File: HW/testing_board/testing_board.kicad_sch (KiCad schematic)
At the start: 66 parts, among them J1 GPIO, J4 Left_, J4 SWD, J5 OLED, J5 Right_, SW1 Start, U1 TPS22917DBV, U2 CD4051BM96, U3 CD4051BM96, U4 CD4051BM96

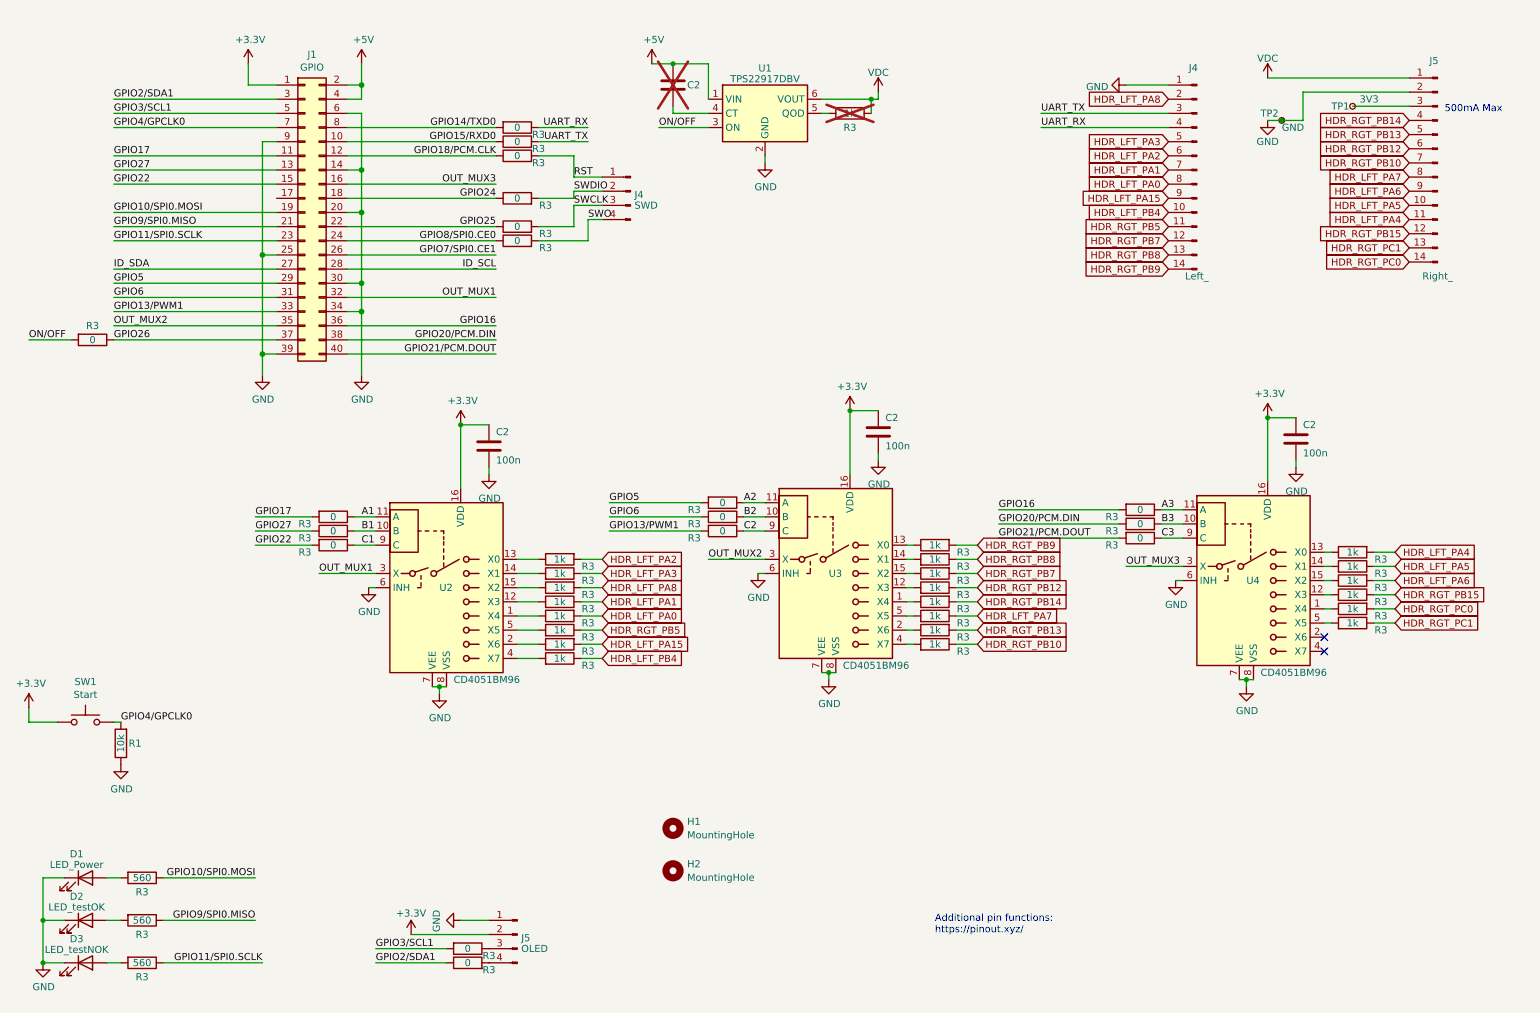
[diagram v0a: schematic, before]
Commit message: add sd card file library+ new HW version
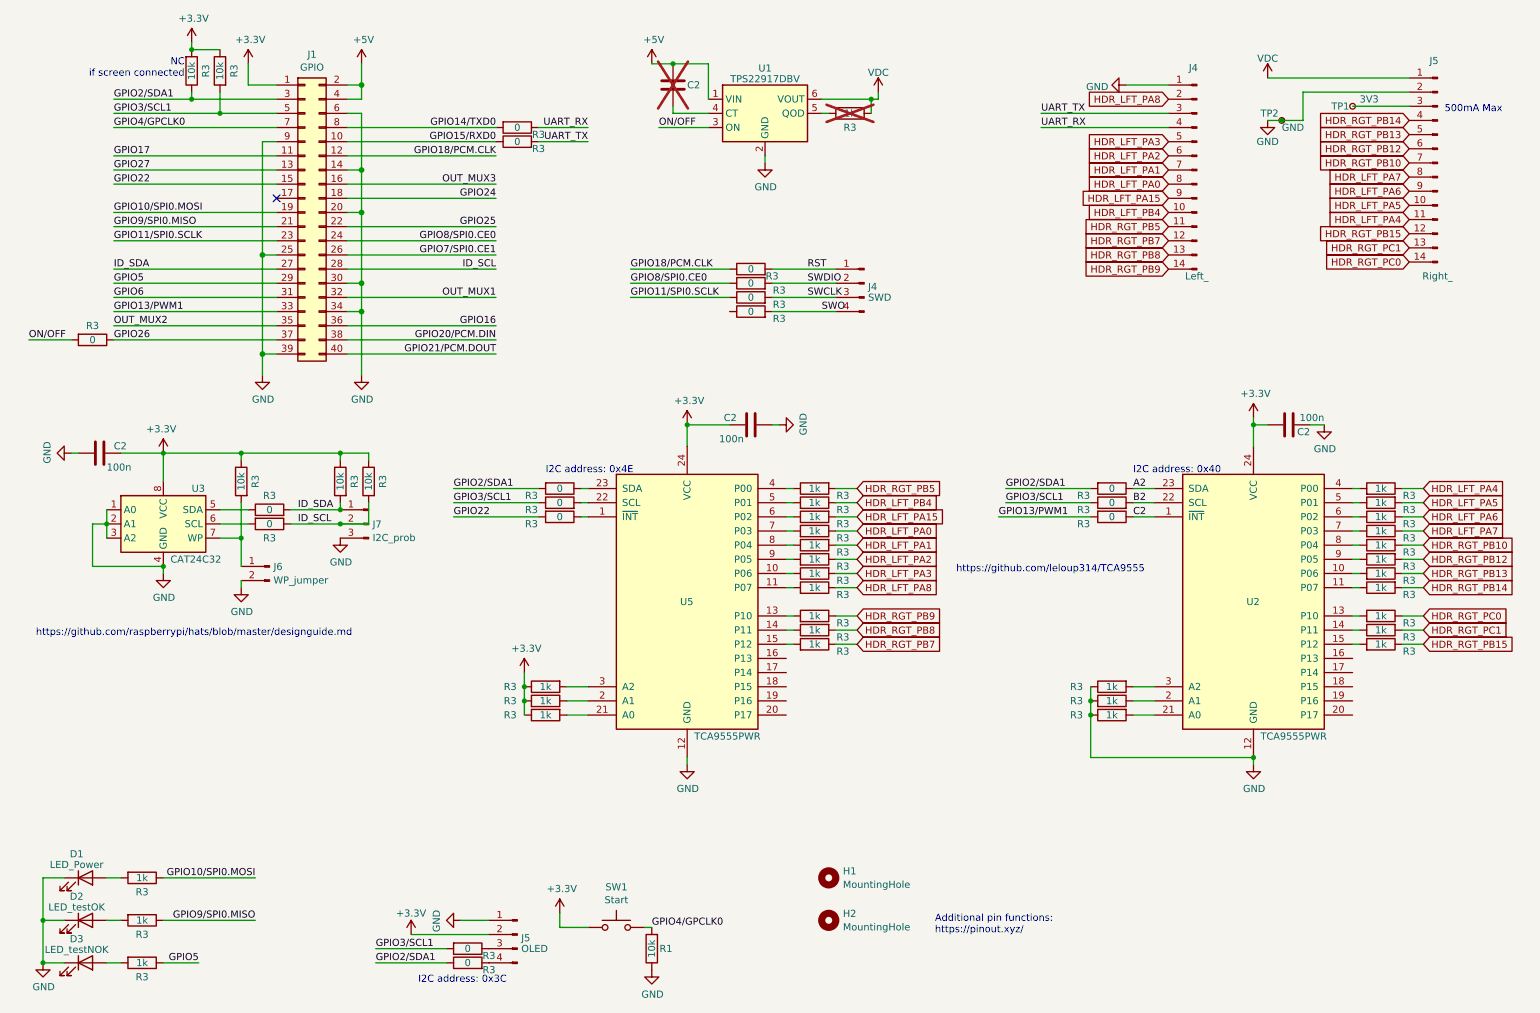
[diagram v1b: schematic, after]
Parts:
- removed R3 (x3): 0, Resistor_SMD:R_0603_1608Metric, symbol Device:R
- removed R3 (x2): 560, Resistor_SMD:R_0603_1608Metric, symbol Device:R
- removed U2, U3, U4: CD4051BM96, Package_SO:SOIC-16_3.9x9.9mm_P1.27mm, symbol Analog_Switch:CD4051B
- added J6: WP_jumper, Connector_PinHeader_2.54mm:PinHeader_1x02_P2.54mm_Vertical, symbol Connector:Conn_01x02_Pin
- added J7: I2C_prob, Connector_PinHeader_2.54mm:PinHeader_1x03_P2.54mm_Vertical, symbol Connector:Conn_01x03_Pin
- added R3 (x5): 10k, Resistor_SMD:R_0603_1608Metric, symbol Device:R
- added R3 (x8): 1k, Resistor_SMD:R_0603_1608Metric, symbol Device:R
- added R3 (x2): 0, Resistor_SMD:R_0603_1608Metric, symbol Device:R
- added U2, U5: TCA9555PWR, Package_SO:TSSOP-24_4.4x7.8mm_P0.65mm, symbol Interface_Expansion:TCA9555PWR
- added U3: CAT24C32, Package_SO:SOIC-8_3.9x4.9mm_P1.27mm, symbol Memory_EEPROM:CAT24C128
- R3: value 560 -> 1k
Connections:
- net +3V3: now also R3.1, R3.1, R3.1, R3.1, R3.1, R3.1, R3.2, R3.2, U2.24 (VCC), U3.8 (VCC), U5.24 (VCC)
- net A2: now also U2.23 (SDA)
- net B2: now also U2.22 (SCL)
- net C2: now also U2.1 (~{INT})
- net GND: now also J6.2 (Pin_2), J7.3 (Pin_3), R3.1, R3.1, R3.2, U2.12 (GND), U3.1 (A0), U3.2 (A1), U3.3 (A2), U3.4 (GND), U5.12 (GND)
- net GPIO11/SPI0.SCLK: now also R3.1
- net GPIO17: no longer R3.2
- net GPIO24: no longer R3.1
- net GPIO25: no longer R3.1
- net GPIO27: no longer R3.1
- net GPIO2/SDA1: now also R3.2, R3.2, R3.1
- net GPIO3/SCL1: now also R3.1, R3.1, R3.2
- net GPIO5: now also R3.1; no longer R3.2
- net GPIO6: no longer R3.1
- net GPIO8/SPI0.CE0: now also R3.1; no longer R3.1
- net GPIO9/SPI0.MISO: now also R3.1
- net HDR_LFT_PA0: now also R3.1; no longer R3.2
- net HDR_LFT_PA1: now also R3.2; no longer R3.1
- net HDR_LFT_PA15: now also R3.2; no longer R3.2
- net HDR_LFT_PA2: now also R3.1; no longer R3.2
- net HDR_LFT_PA3: now also R3.2; no longer R3.1
- net HDR_LFT_PA4: now also R3.1; no longer R3.2
- net HDR_LFT_PA5: now also R3.2; no longer R3.1
- net HDR_LFT_PA6: now also R3.2; no longer R3.2
- net HDR_LFT_PA7: now also R3.1; no longer R3.1
- net HDR_LFT_PA8: now also R3.1; no longer R3.2
- net HDR_LFT_PB4: now also R3.1; no longer R3.1
- net HDR_RGT_PB10: now also R3.2; no longer R3.1
- net HDR_RGT_PB12: now also R3.2; no longer R3.1
- net HDR_RGT_PB13: now also R3.1; no longer R3.2
- net HDR_RGT_PB14: now also R3.2; no longer R3.2
- net HDR_RGT_PB15: now also R3.1; no longer R3.1
- net HDR_RGT_PB5: now also R3.2; no longer R3.1
- net HDR_RGT_PB7: now also R3.1; no longer R3.2
- net HDR_RGT_PB8: now also R3.2; no longer R3.1
- net HDR_RGT_PB9: now also R3.1; no longer R3.2
- net HDR_RGT_PC0: now also R3.1; no longer R3.2
- net HDR_RGT_PC1: now also R3.2; no longer R3.1
- net ID_SCL: now also J7.2 (Pin_2), R3.1, R3.2
- net ID_SDA: now also J7.1 (Pin_1), R3.2, R3.2
- net at R3.1: now also U5.6 (P02)
- net at R3.2: now also U5.11 (P07)
- net at R3.2: now also U5.5 (P01)
- net at R3.1: now also U2.14 (P11)
- net at R3.1: now also U2.5 (P01)
- net at R3.2: now also U2.4 (P00)
- net at R3.1: now also U2.6 (P02)
- net at R3.2: now also U2.7 (P03)
- net at R3.1: now also U2.8 (P04)
- net at R3.1: now also U5.14 (P11)
- net at R3.2: now also U5.15 (P12)
- net at R3.2: now also U5.13 (P10)
- net at R3.2: now also U5.7 (P03)
- net at R3.1: now also U5.8 (P04)
- net at R3.2: now also U2.13 (P10)
- net at R3.2: now also U2.10 (P06)
- net at R3.2: now also U5.9 (P05)
- net at R3.1: now also U2.9 (P05)
- net at R3.1: now also U2.11 (P07)
- net at R3.2: now also U2.15 (P12)
- net at R3.1: now also U5.4 (P00)
- net at R3.1: now also U5.10 (P06)
- net at D2.2 (A): now also R3.2
- net at D3.2 (A): now also R3.2
- net A1: no longer names the net of R3.1
- net A1: now also U5.23 (SDA)
- net B1: no longer names the net of R3.2
- net B1: now also U5.22 (SCL)
- net C1: no longer names the net of R3.1
- net C1: now also U5.1 (~{INT})
- new net: J6.1 (Pin_1), R3.2, U3.7 (WP)
- new net: R3.1, U3.5 (SDA)
- new net: R3.2, U3.6 (SCL)
- new net: R3.2, U2.21 (A0)
- new net: R3.1, U2.2 (A1)
- new net: R3.2, U5.21 (A0)
- new net: R3.1, U5.2 (A1)
- new net: R3.2, U2.3 (A2)
- new net: R3.2, U5.3 (A2)
- no-connect marks 2 -> 1
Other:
- note added: "I2C address: 0x3C"
- note added: "I2C address: 0x40"
- note added: "I2C address: 0x4E"
- note added: "NC if screen connected"
- note added: "https://github.com/leloup314/TCA9555"
- note added: "https://github.com/raspberrypi/hats/blob/master/designguide.md"
- moved on the sheet: C2, H1, H2, J4, R1, R3, SW1
